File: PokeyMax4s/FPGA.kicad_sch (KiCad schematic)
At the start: 11 parts, among them U3 MAX10, X1 50MHz

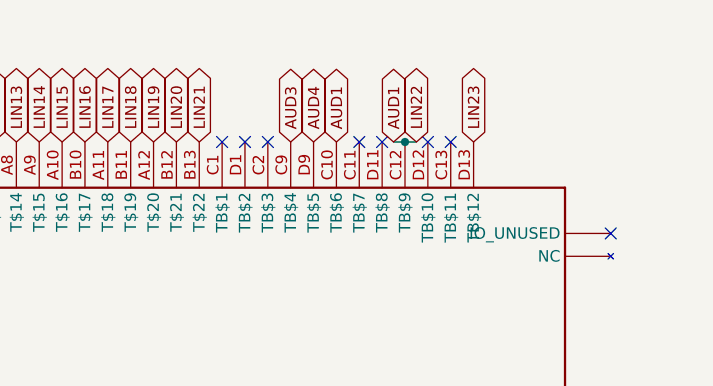
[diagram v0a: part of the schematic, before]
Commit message: Fix LIN22 to AUD1 erroneous connection
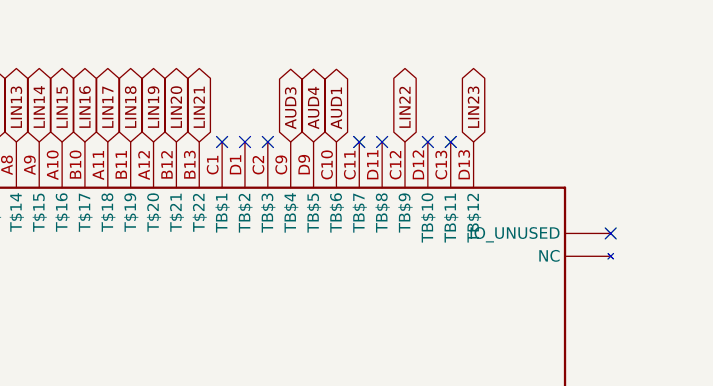
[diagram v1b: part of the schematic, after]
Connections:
- net AUD1: no longer U3.C12 (TB$9)
- new net LIN22: U3.C12 (TB$9)
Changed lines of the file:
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@@
 (kicad_sch
-	(version 20231120)
+	(version 20250114)
 	(generator "eeschema")
-	(generator_version "8.0")
+	(generator_version "9.0")
 	(paper "User" 311.226 210.007)
+	(text "Disable  “Auto-reconfigure from secondary image when initial image fails\""
+		(exclude_from_sim no)
+		(at 157.48 93.98 0)
+		(effects
+			(font
+				(size 1.778 1.5113)
+			)
+			(justify left bottom)
+		)
+	)
+	(text "B16 - L10P/M10N    : P7/THRES\nB14  - K8P/J8N     : --\nB12(TR) - L11P/M11N: ADX_TX, NC\nB11(R)  - N9P/N10N : P6/THRES\nB10(TR) - M12P/M13N: ADC_IN, ADX_RX\nB9 (TR) - K7P/J7P  : --\nB8 (R)  - M9P/M8N  : P5/THRES\nB7 (TR) - K6P/J6N  : --\nB6 (R)  - N8P/N7N  : P4/THRES\nB5 (TR) - M7P/N6N  : P3/THRES\nB4 (R)  - N5P/N4n  : P1/THRES\nB3 (TR) - J5P/K5N  : --\nB2 (R)  - M5P/M4n  : P0/THRES\nB1 (TR) - L4P/L5N  : P2/THRES"
+		(exclude_from_sim no)
+		(at 193.04 139.7 0)
+		(effects
+			(font
+				(size 1.778 1.5113)
+			)
+			(justify left bottom)
+		)
+	)
+	(text "LVDS - bank 3 with 2.5v.  L6,L7,L8"
+		(exclude_from_sim no)
+		(at 144.78 109.22 0)
+		(effects
+			(font
+				(size 1.778 1.5113)
+			)
+			(justify left bottom)
+		)
+	)
+	(text "VCCA, does it need extra filtering? YES (bead...)"
+		(exclude_from_sim no)
+		(at 47.752 123.698 0)
+		(effects
+			(font
+				(size 1.778 1.5113)
+			)
+			(justify left bottom)
+		)
+	)
 	(junction
 		(at 121.92 116.84)
@@
 	)
 	(junction
-		(at 233.68 55.88)
-		(diameter 0)
-		(color 0 0 0 0)
-	)
-	(junction
 		(at 157.48 170.18)
 		(diameter 0)
@@
 	(wire
 		(pts
-			(xy 233.68 55.88) (xy 234.95 55.88)
-		)
-		(stroke
-			(width 0)
-			(type default)
-		)
-	)
-	(wire
-		(pts
 			(xy 114.3 88.9) (xy 114.3 63.5)
 		)
@@
 	(wire
 		(pts
-			(xy 233.68 55.88) (xy 232.41 55.88)
-		)
-		(stroke
-			(width 0)
-			(type default)
-		)
-	)
-	(wire
-		(pts
 			(xy 25.4 172.72) (xy 17.78 172.72)
 		)
@@
 			(width 0.1524)
 			(type solid)
-		)
-	)
-	(text "Disable  “Auto-reconfigure from secondary image when initial image fails\""
-		(exclude_from_sim no)
-		(at 157.48 93.98 0)
-		(effects
-			(font
-				(size 1.778 1.5113)
-			)
-			(justify left bottom)
-		)
-	)
-	(text "B16 - L10P/M10N    : P7/THRES\nB14  - K8P/J8N     : --\nB12(TR) - L11P/M11N: ADX_TX, NC\nB11(R)  - N9P/N10N : P6/THRES\nB10(TR) - M12P/M13N: ADC_IN, ADX_RX\nB9 (TR) - K7P/J7P  : --\nB8 (R)  - M9P/M8N  : P5/THRES\nB7 (TR) - K6P/J6N  : --\nB6 (R)  - N8P/N7N  : P4/THRES\nB5 (TR) - M7P/N6N  : P3/THRES\nB4 (R)  - N5P/N4n  : P1/THRES\nB3 (TR) - J5P/K5N  : --\nB2 (R)  - M5P/M4n  : P0/THRES\nB1 (TR) - L4P/L5N  : P2/THRES"
-		(exclude_from_sim no)
-		(at 193.04 139.7 0)
-		(effects
-			(font
-				(size 1.778 1.5113)
-			)
-			(justify left bottom)
-		)
-	)
-	(text "LVDS - bank 3 with 2.5v.  L6,L7,L8"
-		(exclude_from_sim no)
-		(at 144.78 109.22 0)
-		(effects
-			(font
-				(size 1.778 1.5113)
-			)
-			(justify left bottom)
-		)
-	)
-	(text "VCCA, does it need extra filtering? YES (bead...)"
-		(exclude_from_sim no)
-		(at 47.752 123.698 0)
-		(effects
-			(font
-				(size 1.778 1.5113)
-			)
-			(justify left bottom)
 		)
 	)
 	(label "TMS"
 		(at 129.54 73.66 0)
-		(fields_autoplaced yes)
 		(effects
 			(font
@@
 	(label "TMS"
 		(at 91.44 66.04 0)
-		(fields_autoplaced yes)
 		(effects
 			(font
@@
 	(label "TDI"
 		(at 129.54 76.2 0)
-		(fields_autoplaced yes)
 		(effects
 			(font
@@
 	(label "TCK"
 		(at 129.54 71.12 0)
-		(fields_autoplaced yes)
 		(effects
 			(font
@@
 	(label "OSC_CLOCK"
 		(at 121.92 142.24 0)
-		(fields_autoplaced yes)
 		(effects
 			(font
@@
 	(label "TCK"
 		(at 91.44 71.12 0)
-		(fields_autoplaced yes)
 		(effects
 			(font
@@
 	(label "TDO"
 		(at 91.44 76.2 0)
-		(fields_autoplaced yes)
 		(effects
 			(font
@@
 	(label "TDI"
 		(at 91.44 68.58 0)
-		(fields_autoplaced yes)
 		(effects
 			(font
@@
 	(label "NC1"
 		(at 187.96 160.02 90)
-		(fields_autoplaced yes)
 		(effects
 			(font
@@
 	(label "TDO"
 		(at 129.54 78.74 0)
-		(fields_autoplaced yes)
 		(effects
 			(font
@@
 		)
 	)
-	(global_label "AUD1"
-		(shape bidirectional)
-		(at 232.41 55.88 90)
-		(fields_autoplaced yes)
-		(effects
-			(font
-				(size 1.2446 1.2446)
-			)
-			(justify left)
-		)
-		(property "Intersheetrefs" "${INTERSHEET_REFS}"
-			(at 232.41 46.5911 90)
-			(effects
-				(font
-					(size 1.27 1.27)
-				)
-				(justify left)
-				(hide yes)
-			)
-		)
-	)
 	(global_label "LIN23"
 		(shape bidirectional)
@@
 	(global_label "LIN22"
 		(shape bidirectional)
-		(at 234.95 55.88 90)
-		(fields_autoplaced yes)
-		(effects
-			(font
-				(size 1.2446 1.2446)
-			)
-			(justify left)
-		)
-		(property "Intersheetrefs" "${INTERSHEET_REFS}"
-			(at 234.95 46.5911 90)
-			(effects
-				(font
+		(at 233.68 55.88 90)
+		(fields_autoplaced yes)
+		(effects
+			(font
+				(size 1.2446 1.2446)
+			)
+			(justify left)
+		)
+		(property "Intersheetrefs" "${INTERSHEET_REFS}"
+			(at 233.68 46.5911 90)
+			(effects
+				(font
